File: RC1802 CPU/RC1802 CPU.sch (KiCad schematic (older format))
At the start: 54 parts, among them J1 Mount, J2 Mount, J3 Mount, J4 Mount, J5 Expansion, J6 UI_Connector, J7 BARREL_JACK, J8 ClockPort, J9 Q_Connector, U1 74LS04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

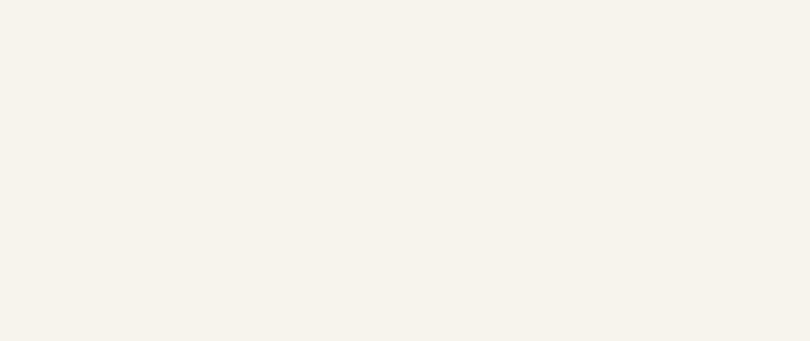
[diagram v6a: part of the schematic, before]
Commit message: Fixed DMA_OUT fault in schematic and layout
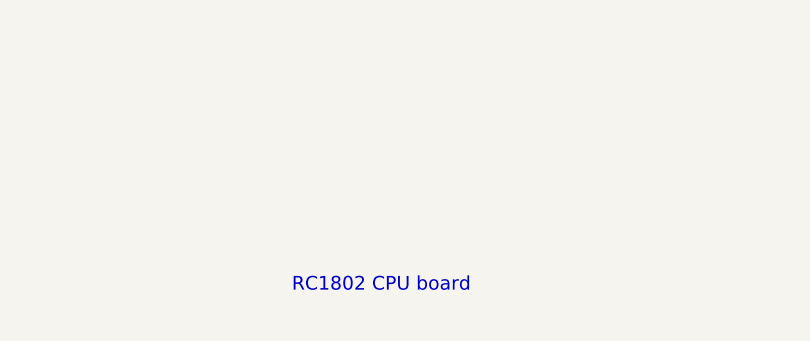
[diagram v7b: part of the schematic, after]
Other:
- note added: "RC1802 CPU board"
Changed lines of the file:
@@
 NoConn ~ 13125 3525
 $Comp
-L VCC #PWR?
+L VCC #PWR026
 U 1 1 5BC737DE
 P 13400 5125
-F 0 "#PWR?" H 13400 4975 50  0001 C CNN
+F 0 "#PWR026" H 13400 4975 50  0001 C CNN
 F 1 "VCC" H 13400 5275 50  0000 C CNN
 F 2 "" H 13400 5125 50  0001 C CNN
@@
 Text GLabel 13125 4725 2    60   Input ~ 0
 CLOCK_OUT
+Text Notes 12200 10925 0    60   ~ 0
+RC1802 CPU board
 $EndSCHEMATC

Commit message: KiCad 5 update, both boards now marked F to match (without any actual changes)
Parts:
- C1, C2, C3, C4, C5, C6: symbol C_Small -> Device:C_Small
- D1, D2, D3, D4, D5, D6, D7, D8: symbol LED_Small -> Device:LED_Small
- D9: symbol D -> Device:D
- J1, J2, J3, J4: symbol CONN_01X01 -> RC1802-CPU-rescue:CONN_01X01
- J5: symbol CONN_01X39 -> RC1802-CPU-rescue:CONN_01X39
- J6: symbol CONN_02X20 -> RC1802-CPU-rescue:CONN_02X20
- J7: symbol BARREL_JACK -> RC1802-CPU-rescue:BARREL_JACK
- J8: symbol Conn_01x05-RESCUE-RC1802_CPU -> RC1802-CPU-rescue:Conn_01x05-RESCUE-RC1802_CPU
- J9: symbol Conn_01x05_Male -> conn:Conn_01x05_Male
- JP1, JP2, JP3, JP4, JP5, JP6, JP7, JP8: symbol Jumper_NC_Dual -> Device:Jumper_NC_Dual
- R1, R10, R11, R12, R13, R14, R15, R2, R3, R4, R5, R6, R7, R8, R9: symbol R -> Device:R
- U1: symbol 74LS04 -> RC1802-CPU-rescue:74LS04
- U2: symbol CDP1802 -> cdp1802:CDP1802
- U3: symbol 74LS240 -> RC1802-CPU-rescue:74LS240
- U4: symbol 74LS373 -> RC1802-CPU-rescue:74LS373
- U5: symbol HM62256BLP-7 -> memory:HM62256BLP-7
- U6: symbol 28C256 -> memory:28C256
- X1: symbol CXO_DIP14 -> Oscillators:CXO_DIP14
